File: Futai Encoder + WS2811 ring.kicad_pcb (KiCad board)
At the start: 2 copper layers, 31.1 x 49 mm, 50 parts, among them J1 Conn_02x05_Top_Bottom, SW1 RotaryEncoder_Switch_RGB

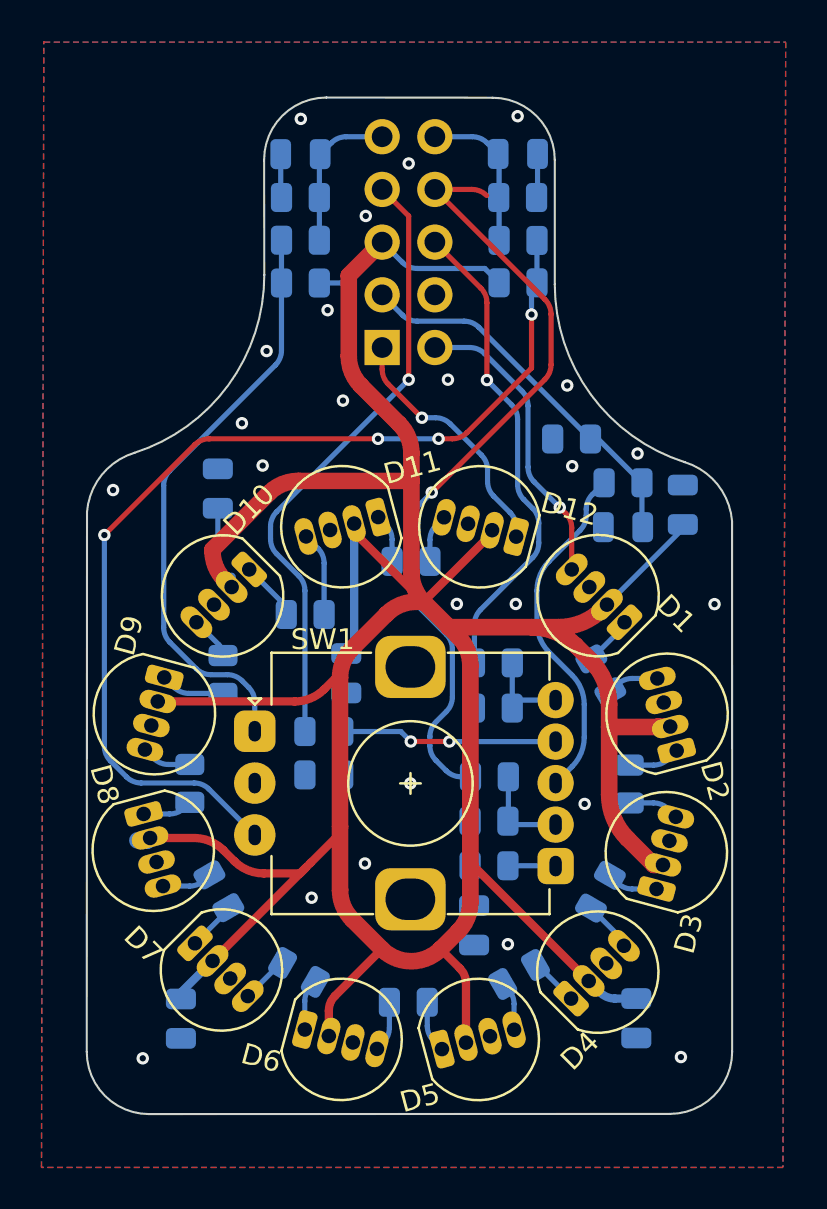
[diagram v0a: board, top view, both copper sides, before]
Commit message: encoder with shorter handle
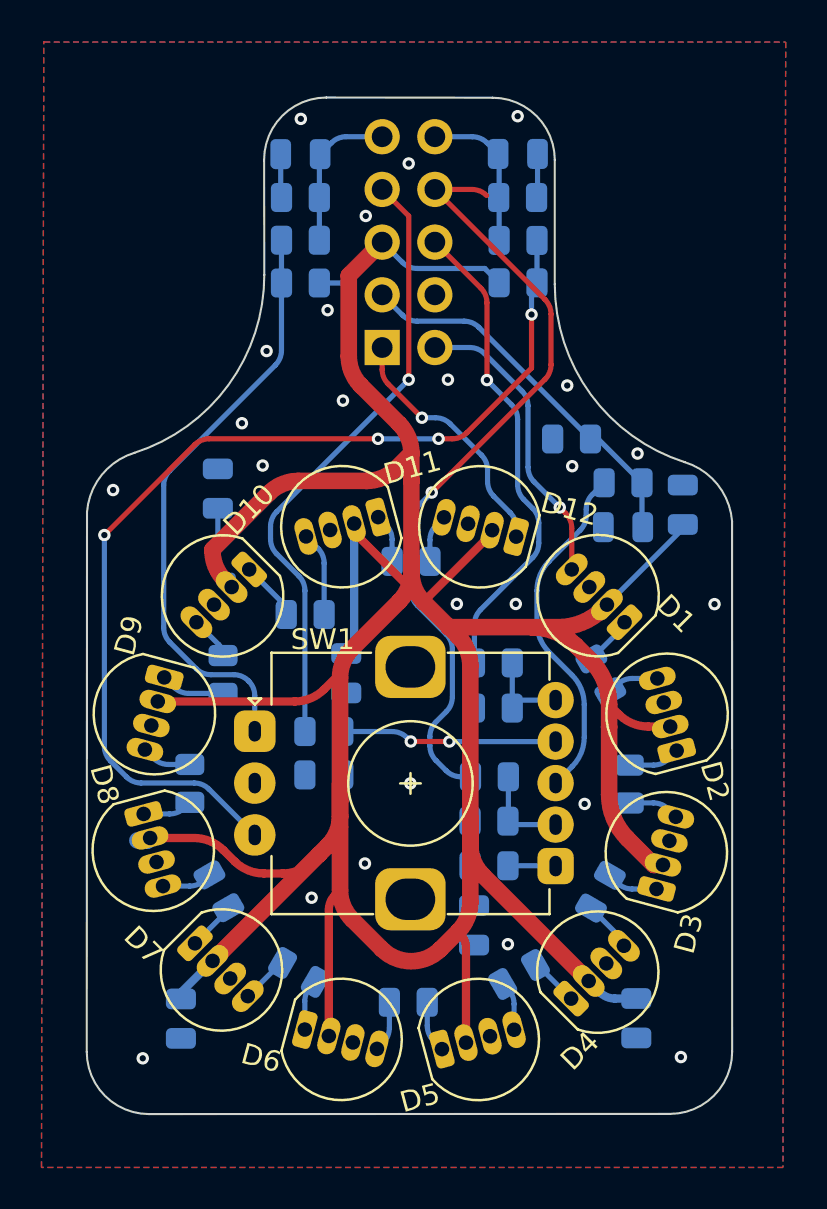
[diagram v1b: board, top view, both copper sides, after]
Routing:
- net +5VL: track 197.0 -> 206.5 mm

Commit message: handsolder friendly footprint for LEDs
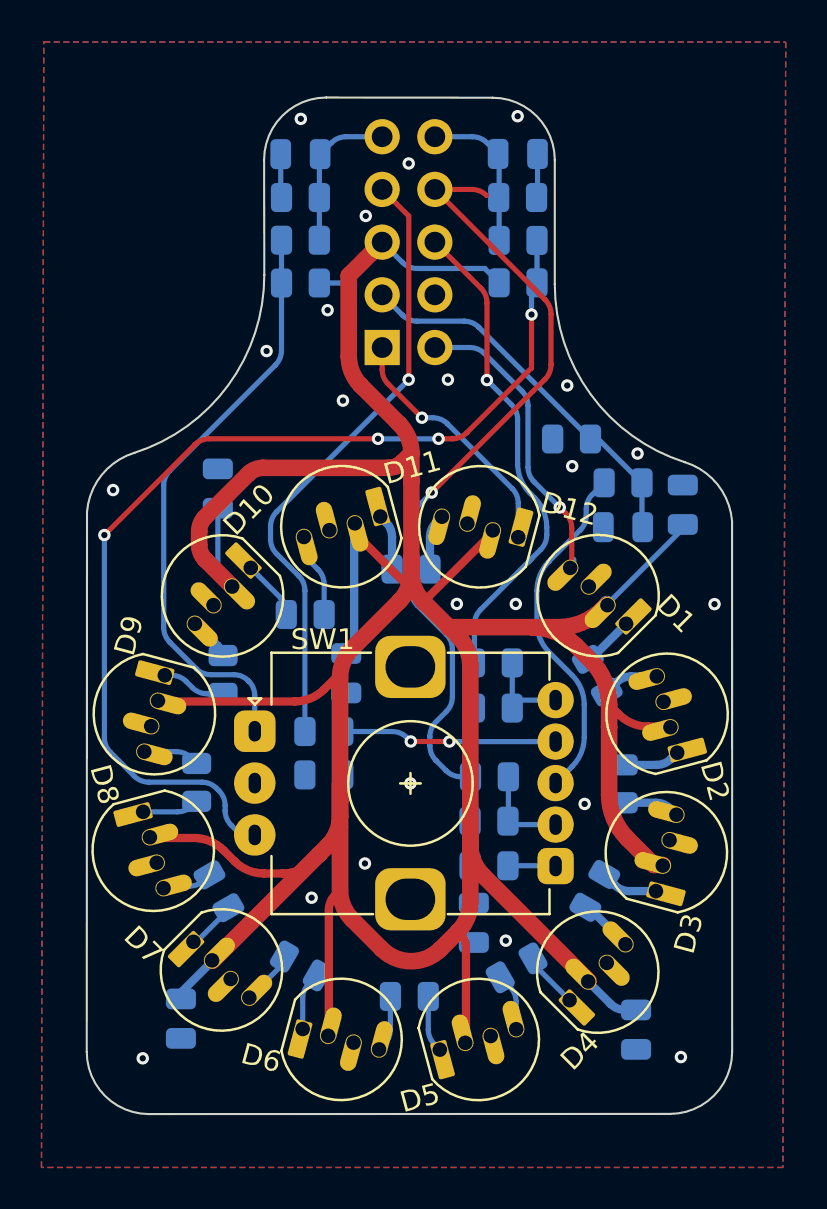
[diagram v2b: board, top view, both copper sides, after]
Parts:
- moved C3 0.55 mm to (145.9, 98.1)
- moved R11 0.37 mm to (135.1, 75.9)
- moved R4 0.34 mm to (140.2, 95.1)
- moved R8 0.33 mm to (124.8, 86.2)
- moved R6 0.32 mm to (129.8, 95.0)
- moved R2 0.29 mm to (145.3, 86.3)
- moved R5 0.28 mm to (135.0, 96.5)
- moved R3 0.27 mm to (143.9, 91.4)
- moved R1 0.17 mm to (144.1, 81.0)
- moved C5 0.12 mm to (138.1, 93.0)
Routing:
- net +5VL: track 206.5 -> 205.6 mm
- net Net-(D9-Pad4): track 2.42 -> 3.31 mm
- net Net-(D6-Pad1): track 2.46 -> 3.13 mm
- net GND: vias 24 -> 22

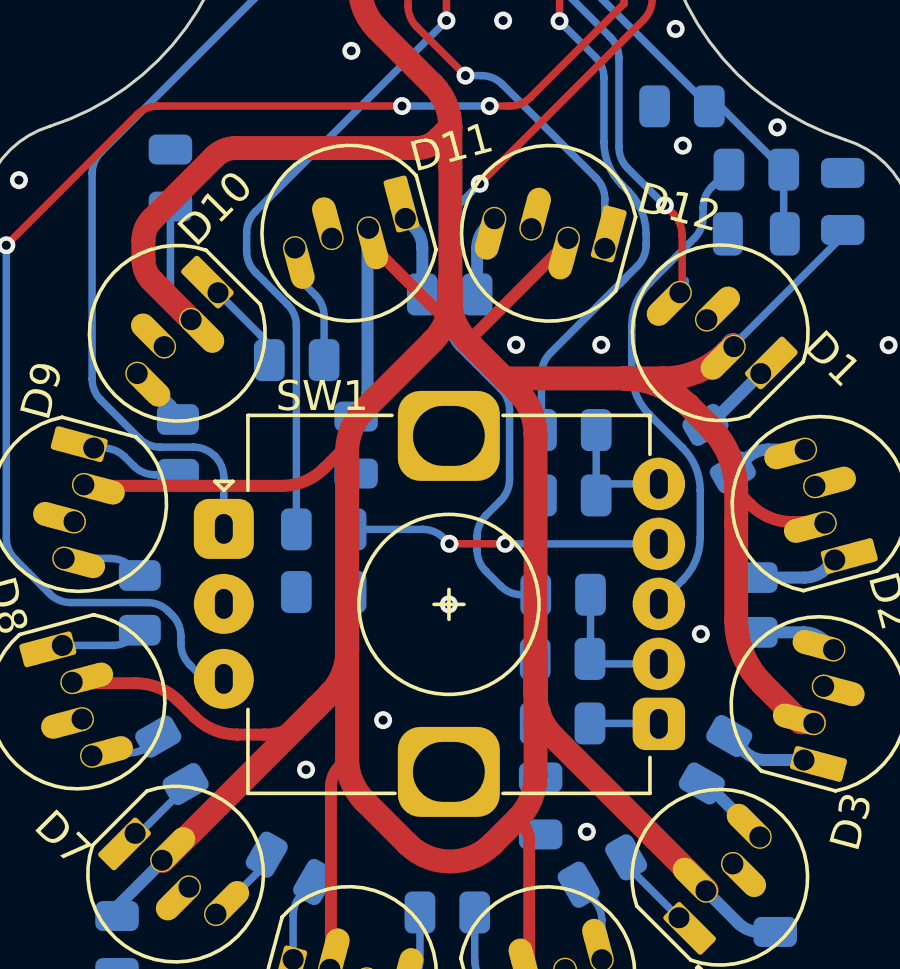
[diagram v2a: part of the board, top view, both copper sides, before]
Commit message: adding M3 hole beneth encoder to mark drill hole on panel
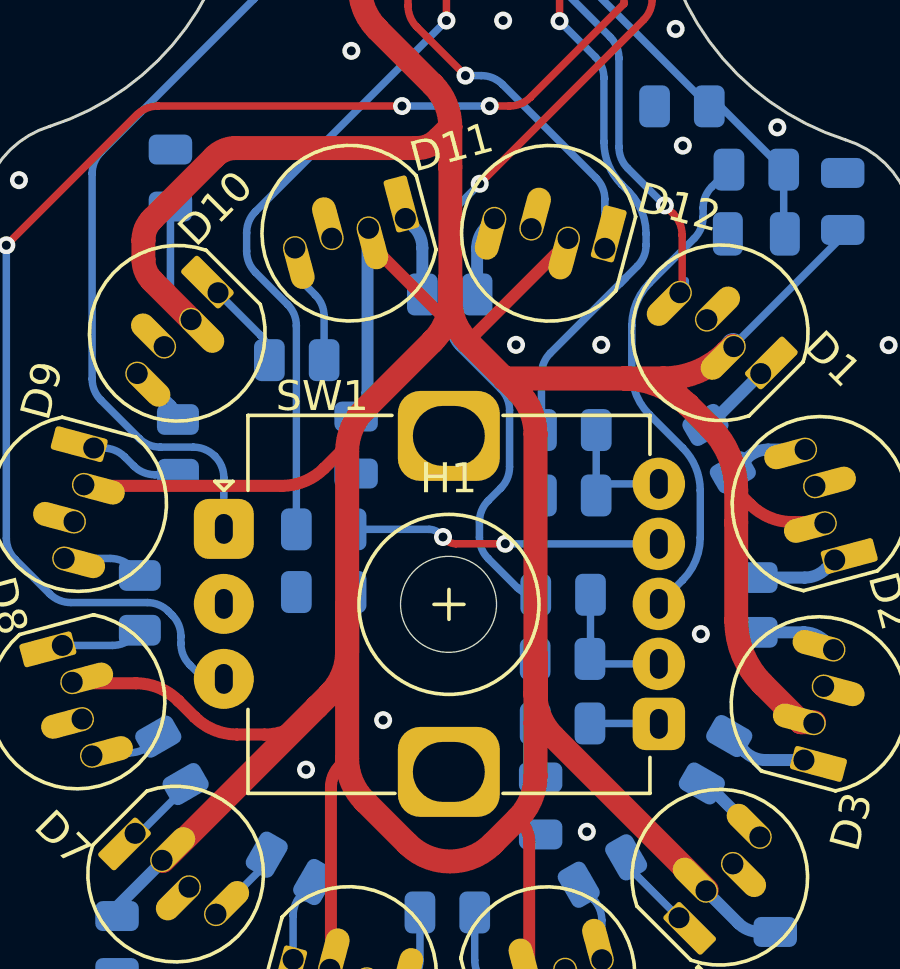
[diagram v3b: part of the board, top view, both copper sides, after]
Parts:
- added H1: MountingHole, andilge KiCad footprints:MountingHole_3.2mm_M3, F.Cu at (135.0, 86.2)
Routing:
- net +5VL: track 205.6 -> 207.5 mm
- net GND: vias 22 -> 21
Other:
- board text added: "v0.92"
- board text removed: "v0.9"

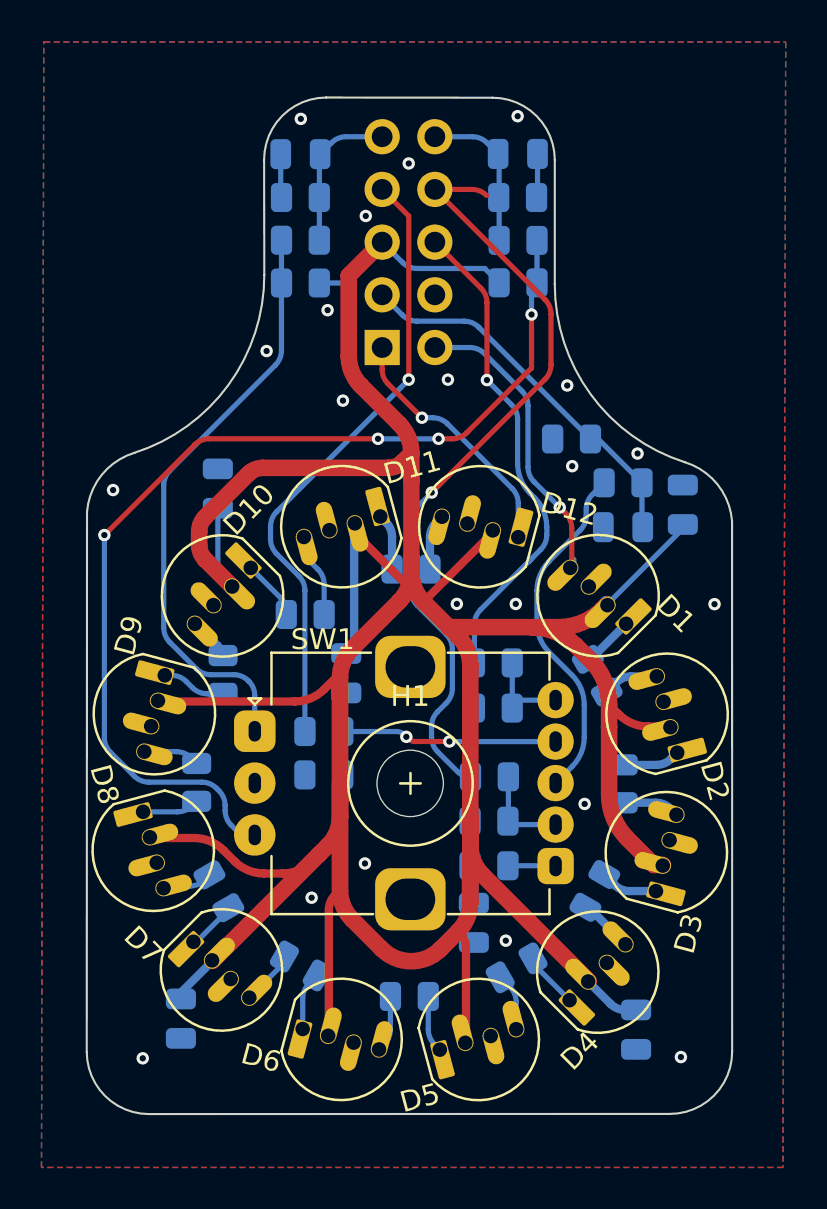
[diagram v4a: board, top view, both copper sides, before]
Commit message: smaller silkscreens, minor changes in trackings
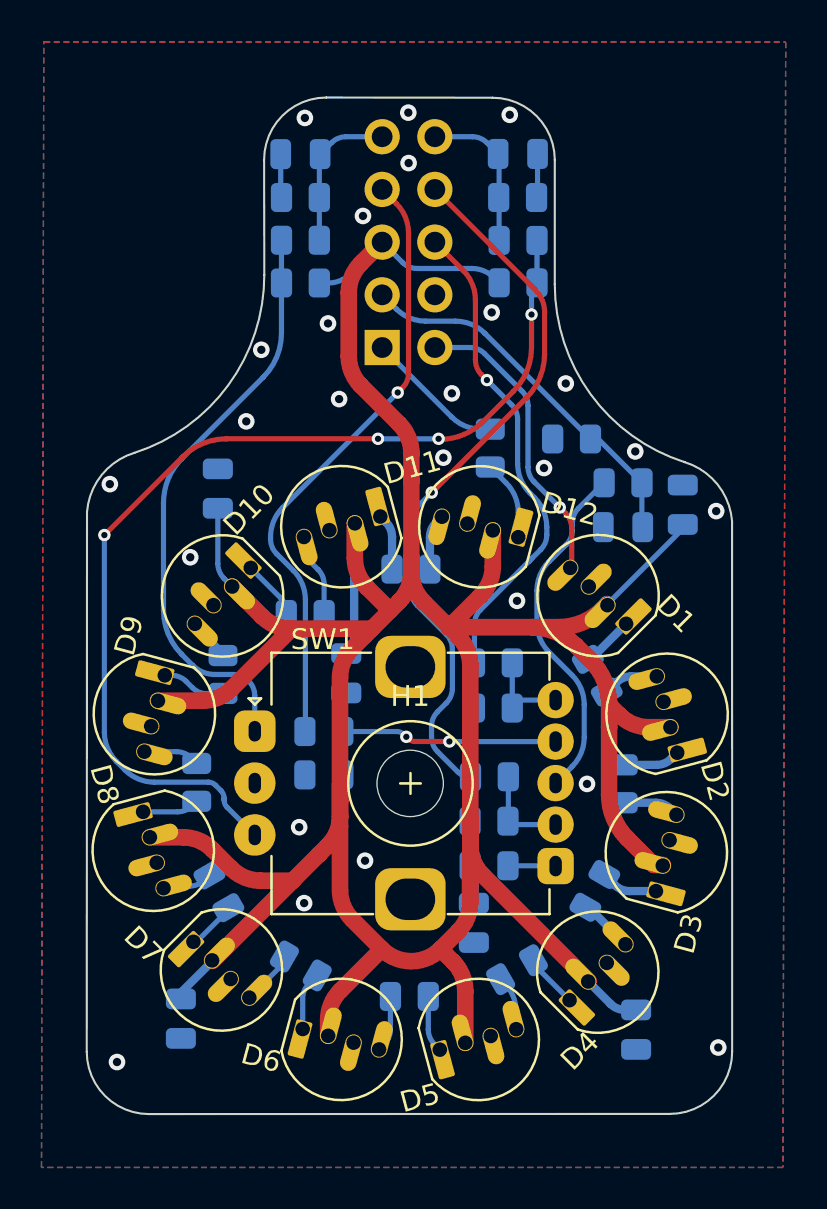
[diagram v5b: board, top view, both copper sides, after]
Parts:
- removed kibuzzard-61EB43D1: G***, kibuzzard-61EB43D1
- added R12: 75Ω, Resistor_SMD:R_0805_2012Metric, B.Cu at (138.9, 70.1)
- added kibuzzard-6202B283: G***, kibuzzard-6202B283, B.Cu at (145.0, 101.1)
- C1, C11, C3, C5, C7, C9: value 220n -> 220nF
- C21: value 100n -> 100nF
- C31, C41: value 10n -> 10nF
- R1, R10, R11, R2, R3, R4, R5, R6, R7, R8, R9: value 75 -> 75Ω
- R21: value 33k -> 33kΩ
- R22: value 68k -> 68kΩ
- R31, R32, R41, R42: value 10k -> 10kΩ
- R33, R43: value 39k -> 39kΩ
- R51, R61, R71: value 12k -> 12kΩ
- R52, R62, R72: value 2k -> 2kΩ
- R81: value 100 -> 100Ω
- moved R4 0.09 mm to (140.2, 95.2)
- turned R3 to -120 degrees
- turned R9 to 90 degrees
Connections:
- D12 pad 1: DOUT -> Net-(D12-Pad1)
- R3 pad 1: Net-(D4-Pad4) -> Net-(D3-Pad1)
- R3 pad 2: Net-(D3-Pad1) -> Net-(D4-Pad4)
- R9 pad 1: Net-(D10-Pad4) -> Net-(D9-Pad1)
- R9 pad 2: Net-(D9-Pad1) -> Net-(D10-Pad4)
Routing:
- net +5VL: track 207.5 -> 194.4 mm
- net DOUT: track 12.3 -> 6.74 mm, vias 1 -> 0
- net Net-(D12-Pad1): track 0.00 -> 3.85 mm
- net Q-BLU: track 37.8 -> 34.9 mm
- net DIN: track 15.1 -> 14.5 mm
- net GND: vias 21 -> 25
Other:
- board text added: "github.com/andilge"
- board text removed: "https://github.com/andilge"

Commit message: fixing typo
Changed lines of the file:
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@@
     (fp_line (start 1 -0.625) (end -1 -0.625) (layer "B.Fab") (width 0.1))
     (fp_line (start 1 0.625) (end 1 -0.625) (layer "B.Fab") (width 0.1))
-    (pad "1" smd roundrect (at -0.9125 0 90) (size 1.025 1.4) (layers "B.Cu" "B.Paste" "B.Mask") (roundrect_rratio 0.243902)
+    (pad "1" smd roundrect (at -0.9125 0 90) (size 1.025 1.4) (layers "B.Cu" "B.Paste" "B.Mask") (roundrect_rratio 0.243902439)
       (net 40 "Net-(D12-Pad1)") (pintype "passive"))
-    (pad "2" smd roundrect (at 0.9125 0 90) (size 1.025 1.4) (layers "B.Cu" "B.Paste" "B.Mask") (roundrect_rratio 0.243902)
+    (pad "2" smd roundrect (at 0.9125 0 90) (size 1.025 1.4) (layers "B.Cu" "B.Paste" "B.Mask") (roundrect_rratio 0.243902439)
       (net 15 "DOUT") (pintype "passive"))
     (model "${KICAD6_3DMODEL_DIR}/Resistor_SMD.3dshapes/R_0805_2012Metric.wrl"

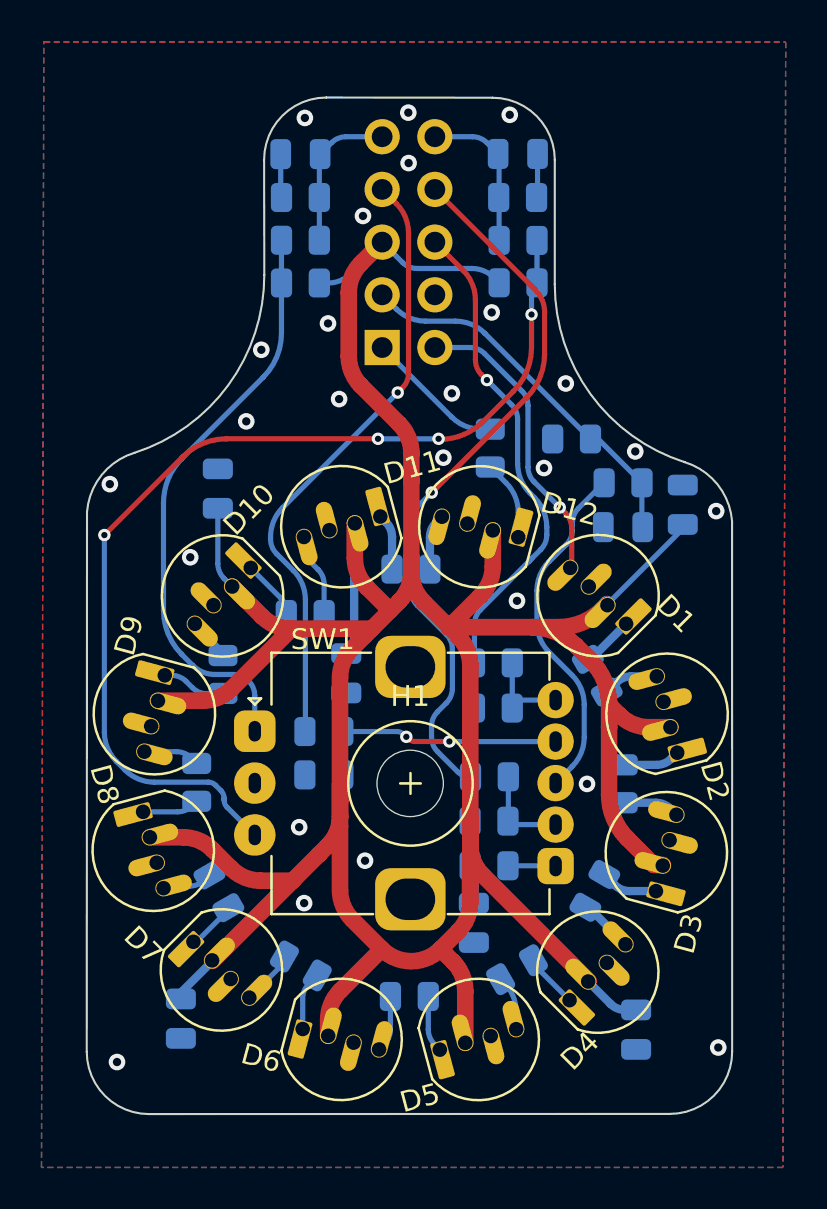
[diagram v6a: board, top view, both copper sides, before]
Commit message: v0.93, minor routing changes, better gnd zones
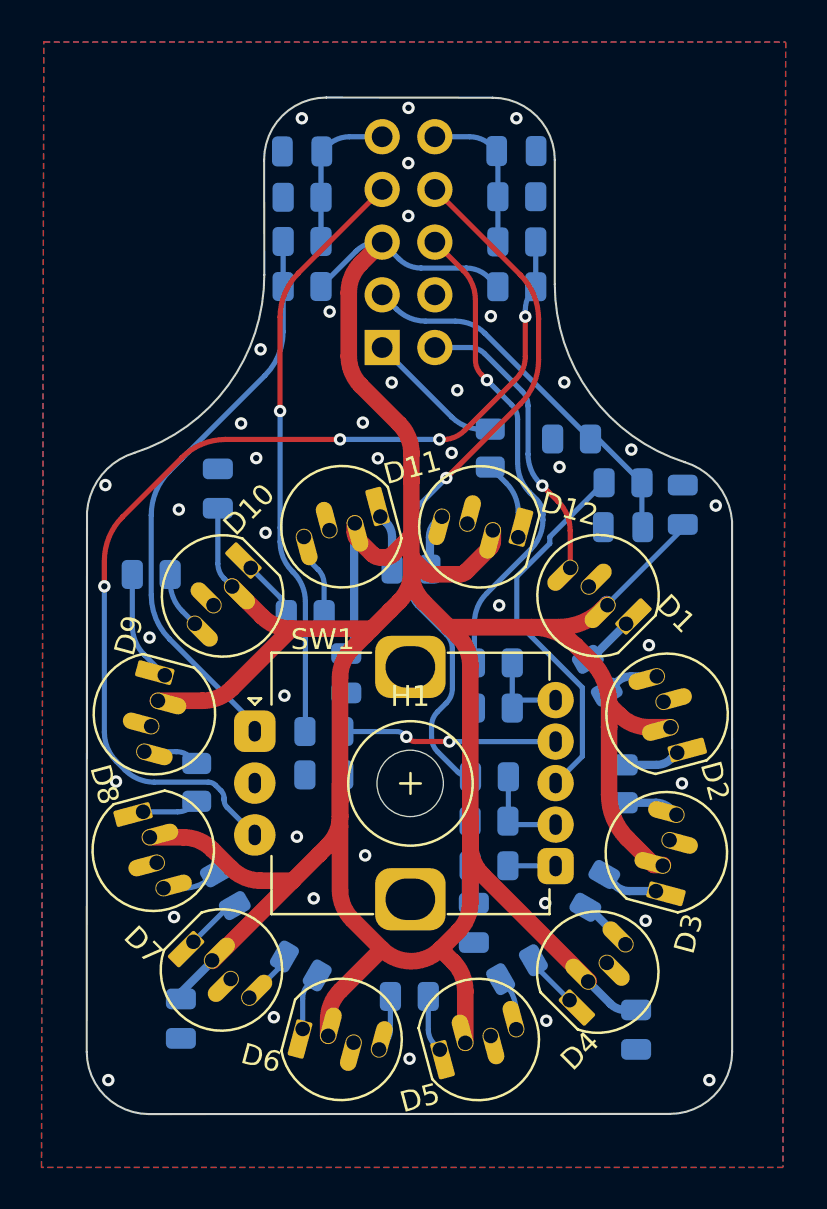
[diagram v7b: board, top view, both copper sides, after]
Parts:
- moved R9 5.93 mm to (122.6, 76.2), turned to 0 degrees
- moved R7 0.33 mm to (126.1, 91.3)
- moved R41 0.20 mm to (140.2, 62.3)
- moved R31 0.19 mm to (129.8, 62.3)
- moved C41 0.16 mm to (140.2, 55.8)
- moved C31 0.15 mm to (129.8, 55.8)
- moved R32 0.10 mm to (129.8, 60.1)
- moved R42 0.09 mm to (140.2, 60.1)
- moved R33 0.08 mm to (129.8, 58.0)
- moved R43 0.06 mm to (140.2, 58.0)
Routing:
- net GND: track 5.90 -> 1.68 mm, vias 25 -> 39
- net Net-(D9-Pad1): track 3.09 -> 5.41 mm
- net Q-GRE: track 29.7 -> 28.3 mm
- net SWC: track 16.9 -> 18.2 mm
- net Net-(D10-Pad4): track 2.09 -> 2.77 mm
- net ENC_A: track 28.4 -> 27.9 mm
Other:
- board text added: "v0.93"
- board text removed: "v0.92"
